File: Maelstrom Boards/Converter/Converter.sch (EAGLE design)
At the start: 37 parts, among them Q1 BSS295, Q2 BSS295, Q3 BSS295

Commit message: Began routing on converter board
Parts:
- removed 12V_OUT, BALANCDIN, MOBO: 39-30-06, con-molex-mini-fit:39-30-06
- removed C1, C6: 1000 uF, rcl:CPOL-USE5-13
- added 12V_LED, 3.3V_LED, 5V_LED: (no value), led:LEDCHIPLED-0603-TTW
- added 1C, 1C1, 1C2: ACS722, ACS722:ACS722
- added C16, C17, C18, C19: (no value), rcl:C-EUC0603
- added P1: 39-30-06, con-molex-mini-fit:39-30-06
- added Q10, Q8, Q9: FDD4141TO252, transistor-fet:FDD4141TO252
- added Q4, Q5: VN10KM, transistor-fet:VN10KM
- added Q6: BSS123, transistor-small-signal:BSS123
- added R10, R11, R12: (no value), rcl:R-US_R0603
- added R13, R14, R15, R16, R17, R18, R19, R20: (no value), resistor:R-US_R0603
- added R21: (no value), resistor:R-US_M2309
- added U$2: ADC128D818, ADC128D818:ADC128D818
- added U$3: 6PIN-VERT, Vertical_Connectors:6PIN-VERT
- Q1: value BSS295 -> VN10KM; device transistor-fet:BSS295 -> transistor-fet:VN10KM
- Q2, Q3: value BSS295 -> BSS123; device transistor-fet:BSS295 -> transistor-small-signal:BSS123
- R4: value 4.47 K -> 4.95 K
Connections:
- removed net 3.3VFILTERED: 3.3VCONVERTER.1,VIN(+), C7.+, L2.2
- new net 12VMONITORED: 12VCONVERTER.1,VIN(+), 1C1.IP-1, 1C1.IP-2
- new net 3V3FILTERED: 1C2.IP+1, 1C2.IP+2, C7.+, L2.2
- new net 3V3MONITORED: 1C2.IP-1, 1C2.IP-2, 3.3VCONVERTER.1,VIN(+)
- new net 5VMONITORED: 1C.IP-1, 1C.IP-2, 5VCONVERTER.1,VIN(+)
- new net JETSON_ON/OFF: Q6.G, U$1.JETSON_ON/OFF
- new net JETSON_SWITCHED: P1.2, Q10.D
- new net MOBO_ON/OFF: Q3.G, U$1.MOBO_ON/OFF
- new net MOBO_SWITCHED: P1.1, Q9.D
- new net N$10: Q8.S, R17.2, R20.1, R21.1
- new net N$11: 1C.VIOUT, U$2.IN2
- new net N$12: 1C1.VIOUT, U$2.IN1
- new net N$13: 1C2.VIOUT, U$2.IN0
- new net N$14: Q10.G, Q6.D, R19.1
- new net N$44: R13.2, R14.1, U$2.A0
- new net N$46: R15.1, R16.2, U$2.A1
- new net N$5: 12V_LED.A, R10.1
- new net N$6: 5V_LED.A, R11.1
- new net N$7: 3.3V_LED.A, R12.1
- new net N$8: Q2.D, Q8.G, R17.1
- new net N$9: Q3.D, Q9.G, R18.1
- new net PLTA_ON/OFF: Q2.G, U$1.CONTROL_SIGNAL
- new net PLTA_SWITCHED: Q8.D, U$1.PLTA_ON/OFF
- new net SCL: U$1.BACKPLANE_SCL, U$2.SCL
- new net SDA: U$1.BACKPLANE_SDA, U$2.SDA
- net +12V: now also P1.4, Q10.S, Q9.S, R10.2, R18.2, R19.2, R21.2; no longer 12V_OUT.1, 12V_OUT.2, 12V_OUT.3, MOBO.1, MOBO.2, MOBO.3
- net +3V3: now also 1C.VCC, 1C1.VCC, 1C2.VCC, C16.1, C17.2, C18.2, C19.2, P1.5, R12.2, R13.1, R16.1, U$2.V+
- net +5V: now also P1.3, R11.2, R20.2
- net 12VFILTERED: now also 1C1.IP+1, 1C1.IP+2; no longer 12VCONVERTER.1,VIN(+)
- net 3.3VON: now also Q5.G; no longer Q3.G
- net 3.3VON-CON: now also Q5.D; no longer Q3.D
- net 5VFILTERED: now also 1C.IP+1, 1C.IP+2; no longer 5VCONVERTER.1,VIN(+)
- net 5VON: now also Q4.G; no longer Q2.G
- net 5VON-CON: now also Q4.D; no longer Q2.D
- net AGND: now also 12V_LED.C, 1C.BW_SEL, 1C.GND, 1C1.BW_SEL, 1C1.GND, 1C2.BW_SEL, 1C2.GND, 3.3V_LED.C, 5V_LED.C, C16.2, C17.1, C18.1, C19.1, P1.6, Q4.S, Q5.S, Q6.S, R14.2, R15.2, U$2.GND, U$3.1+, U$3.1-, U$3.2-; no longer 12V_OUT.4, 12V_OUT.5, 12V_OUT.6, BALANCDIN.4, BALANCDIN.5, BALANCDIN.6, C1.-, C6.-, MOBO.4, MOBO.5, MOBO.6
- net V+: now also U$3.2+, U$3.3+, U$3.3-; no longer BALANCDIN.1, BALANCDIN.2, BALANCDIN.3, C1.+, C6.+

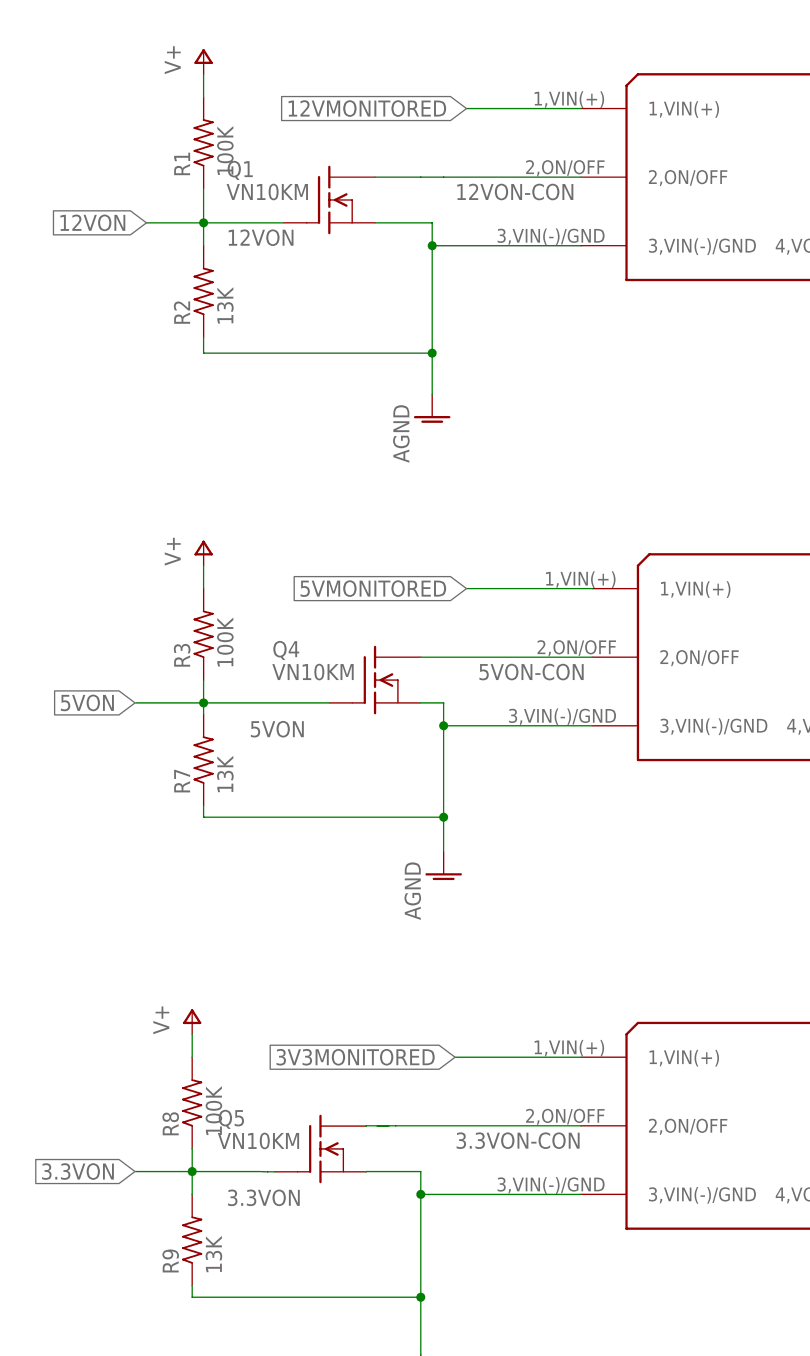
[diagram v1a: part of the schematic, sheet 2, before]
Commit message: Converter board completed
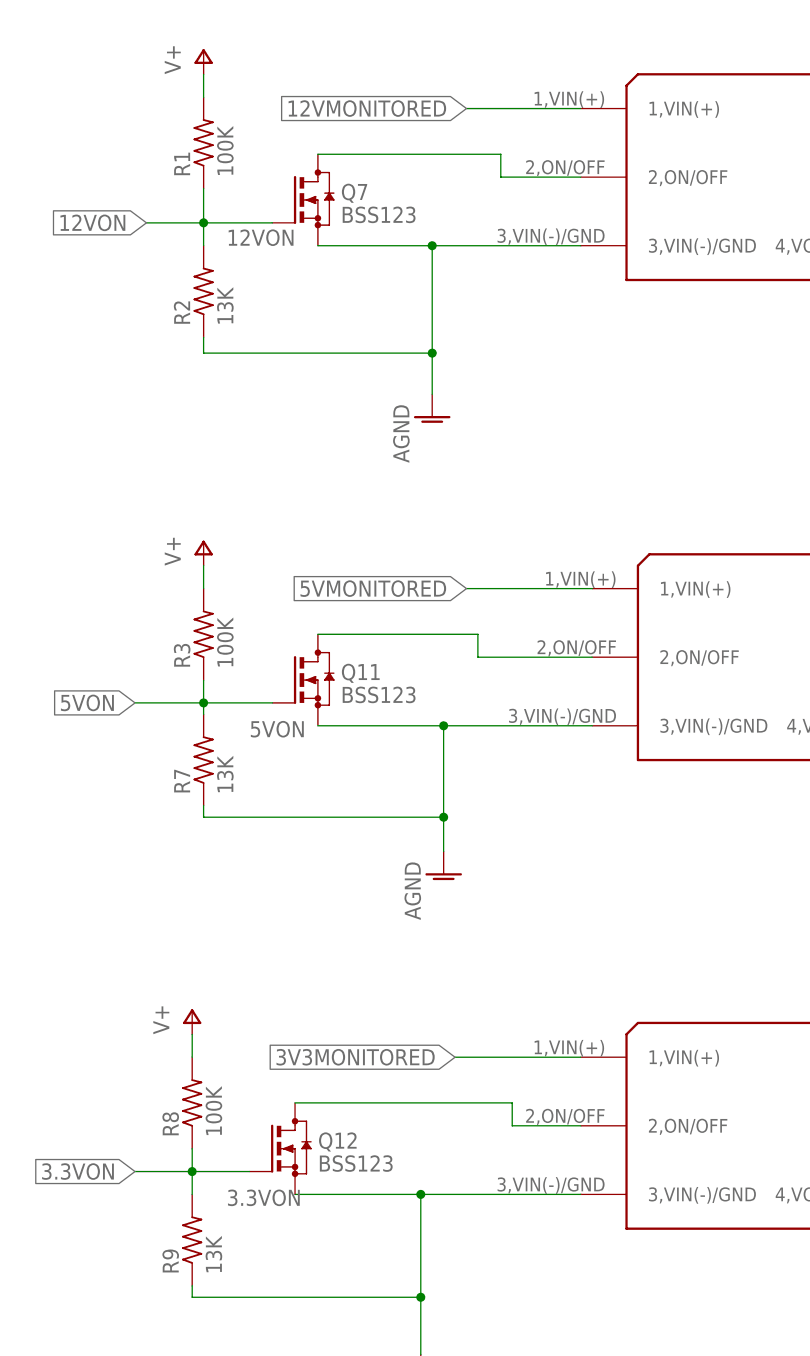
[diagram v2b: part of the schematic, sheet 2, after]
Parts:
- removed Q1, Q4, Q5: VN10KM, transistor-fet:VN10KM
- added Q11, Q12, Q7: BSS123, transistor-small-signal:BSS123
- added R22: (no value), resistor:R-US_M2309
- added R23, R24, R25, R26, R27: (no value), resistor:R-US_R0603
- 12V_LED, 3.3V_LED, 5V_LED: device led:LEDCHIPLED-0603-TTW -> led:LEDCHIPLED_0603
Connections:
- removed net 12VON-CON: 12VCONVERTER.2,ON/OFF, Q1.D
- removed net 3.3VON-CON: 3.3VCONVERTER.2,ON/OFF, Q5.D
- removed net 5VON-CON: 5VCONVERTER.2,ON/OFF, Q4.D
- new net N$15: R20.1, R23.1, U$2.IN3
- new net N$16: R24.1, R26.1, U$2.IN4
- new net N$17: R25.1, R27.1, U$2.IN5
- new net N$18: 12VCONVERTER.2,ON/OFF, Q7.D
- new net N$19: 5VCONVERTER.2,ON/OFF, Q11.D
- new net N$4: 3.3VCONVERTER.2,ON/OFF, Q12.D
- net +12V: now also R20.2
- net +3V3: now also R25.2
- net +5V: now also R22.2, R24.2; no longer R20.2
- net 12VON: now also Q7.G; no longer Q1.G
- net 3.3VON: now also Q12.G; no longer Q5.G
- net 5VON: now also Q11.G; no longer Q4.G
- net AGND: now also Q11.S, Q12.S, Q7.S, R23.2, R26.2, R27.2; no longer Q1.S, Q4.S, Q5.S
- net N$10: now also R22.1; no longer R20.1
- net N$11: now also U$2.IN0; no longer U$2.IN2
- net N$12: now also U$2.IN2; no longer U$2.IN1
- net N$13: now also U$2.IN1; no longer U$2.IN0
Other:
- moved on the sheet: R20
